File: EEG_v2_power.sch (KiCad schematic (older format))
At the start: 13 parts, among them U2 TLV70033, U3 LM2664, U4 TLV70025, U5 TPS72325

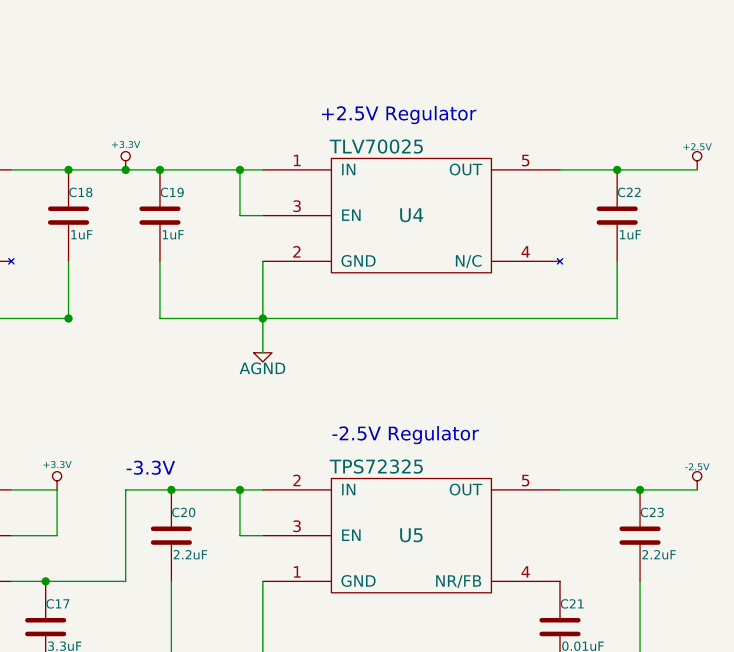
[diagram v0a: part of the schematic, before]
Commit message: Add symbol and footprints for SMD test points.
Add test points to power supplies.
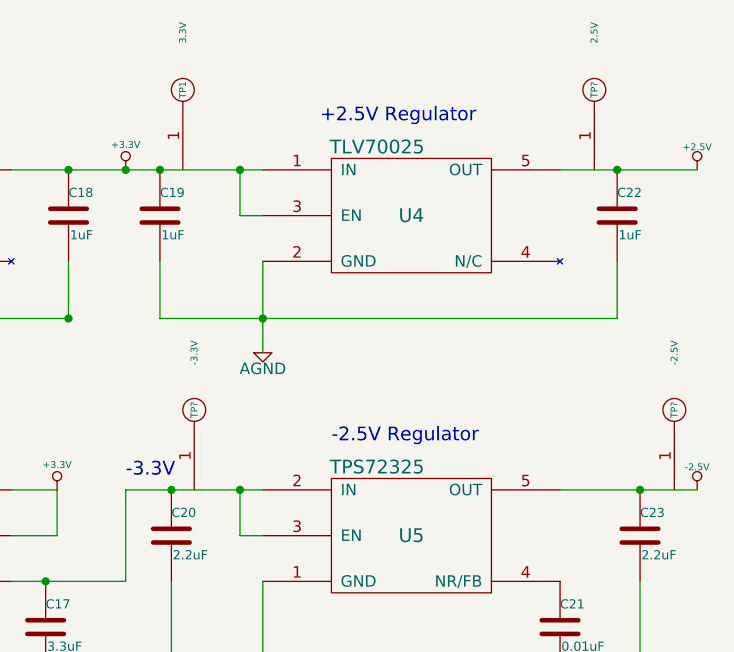
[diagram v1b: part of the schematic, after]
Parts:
- added TP1: 3.3V, ~, symbol SMD_1PIN_PAD
- added TP?: 2.5V, ~, symbol SMD_1PIN_PAD
- added TP?: -3.3V, ~, symbol SMD_1PIN_PAD
- added TP?: -2.5V, ~, symbol SMD_1PIN_PAD
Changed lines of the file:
@@
 +3.3V Regulator
 $Comp
-L +3.3V #PWR19
+L +3.3V #PWR22
 U 1 1 54B47F4F
 P 6450 3050
-F 0 "#PWR19" H 6450 3010 30  0001 C CNN
+F 0 "#PWR22" H 6450 3010 30  0001 C CNN
 F 1 "+3.3V" H 6450 3160 30  0000 C CNN
 F 2 "~" H 6450 3050 60  0000 C CNN
@@
 $EndComp
 $Comp
-L AGND #PWR15
+L AGND #PWR18
 U 1 1 54B47F55
 P 4650 3850
-F 0 "#PWR15" H 4650 3850 40  0001 C CNN
+F 0 "#PWR18" H 4650 3850 40  0001 C CNN
 F 1 "AGND" H 4650 3780 50  0000 C CNN
 F 2 "~" H 4650 3850 60  0000 C CNN
@@
 $EndComp
 $Comp
-L AGND #PWR20
+L AGND #PWR23
 U 1 1 54B47F6D
 P 7050 3850
-F 0 "#PWR20" H 7050 3850 40  0001 C CNN
+F 0 "#PWR23" H 7050 3850 40  0001 C CNN
 F 1 "AGND" H 7050 3780 50  0000 C CNN
 F 2 "~" H 7050 3850 60  0000 C CNN
@@
 $EndComp
 $Comp
-L +2.5V #PWR22
+L +2.5V #PWR25
 U 1 1 54B47F79
 P 8950 3050
-F 0 "#PWR22" H 8950 3000 20  0001 C CNN
+F 0 "#PWR25" H 8950 3000 20  0001 C CNN
 F 1 "+2.5V" H 8950 3150 30  0000 C CNN
 F 2 "" H 8950 3050 60  0000 C CNN
@@
 $EndComp
 $Comp
-L AGND #PWR16
+L AGND #PWR19
 U 1 1 54B47F86
 P 4650 5050
-F 0 "#PWR16" H 4650 5050 40  0001 C CNN
+F 0 "#PWR19" H 4650 5050 40  0001 C CNN
 F 1 "AGND" H 4650 4980 50  0000 C CNN
 F 2 "~" H 4650 5050 60  0000 C CNN
@@
 $EndComp
 $Comp
-L AGND #PWR17
+L AGND #PWR20
 U 1 1 54B47F92
 P 6100 5250
-F 0 "#PWR17" H 6100 5250 40  0001 C CNN
+F 0 "#PWR20" H 6100 5250 40  0001 C CNN
 F 1 "AGND" H 6100 5180 50  0000 C CNN
 F 2 "~" H 6100 5250 60  0000 C CNN
@@
 $EndComp
 $Comp
-L +3.3V #PWR18
+L +3.3V #PWR21
 U 1 1 54B47F98
 P 6150 4450
-F 0 "#PWR18" H 6150 4410 30  0001 C CNN
+F 0 "#PWR21" H 6150 4410 30  0001 C CNN
 F 1 "+3.3V" H 6150 4560 30  0000 C CNN
 F 2 "~" H 6150 4450 60  0000 C CNN
@@
 $EndComp
 $Comp
-L AGND #PWR21
+L AGND #PWR24
 U 1 1 54B47FB2
 P 7650 5350
-F 0 "#PWR21" H 7650 5350 40  0001 C CNN
+F 0 "#PWR24" H 7650 5350 40  0001 C CNN
 F 1 "AGND" H 7650 5280 50  0000 C CNN
 F 2 "~" H 7650 5350 60  0000 C CNN
@@
 $EndComp
 $Comp
-L -2.5V #PWR23
+L -2.5V #PWR26
 U 1 1 54B47FB8
 P 8950 4450
-F 0 "#PWR23" H 8950 4400 20  0001 C CNN
+F 0 "#PWR26" H 8950 4400 20  0001 C CNN
 F 1 "-2.5V" H 8950 4550 30  0000 C CNN
 F 2 "" H 8950 4450 60  0000 C CNN
@@
 Text HLabel 2950 3050 0    60   UnSpc ~ 0
 VIN_RAW
+$Comp
+L SMD_1PIN_PAD TP1
+U 1 1 54C4B7B8
+P 6700 2700
+F 0 "TP1" H 6700 2700 30  0000 C CNN
+F 1 "3.3V" H 6950 2700 30  0000 C CNN
+F 2 "~" H 6700 2700 60  0000 C CNN
+F 3 "~" H 6700 2700 60  0000 C CNN
+	1    6700 2700
+	0    -1   -1   0
+$EndComp
+$Comp
+L SMD_1PIN_PAD TP?
+U 1 1 54C4B7DE
+P 8500 2700
+F 0 "TP?" H 8500 2700 30  0000 C CNN
+F 1 "2.5V" H 8750 2700 30  0000 C CNN
+F 2 "~" H 8500 2700 60  0000 C CNN
+F 3 "~" H 8500 2700 60  0000 C CNN
+	1    8500 2700
+	0    -1   -1   0
+$EndComp
+$Comp
+L SMD_1PIN_PAD TP?
+U 1 1 54C4B7E9
+P 6750 4100
+F 0 "TP?" H 6750 4100 30  0000 C CNN
+F 1 "-3.3V" H 7000 4100 30  0000 C CNN
+F 2 "~" H 6750 4100 60  0000 C CNN
+F 3 "~" H 6750 4100 60  0000 C CNN
+	1    6750 4100
+	0    -1   -1   0
+$EndComp
+$Comp
+L SMD_1PIN_PAD TP?
+U 1 1 54C4B7F4
+P 8850 4100
+F 0 "TP?" H 8850 4100 30  0000 C CNN
+F 1 "-2.5V" H 9100 4100 30  0000 C CNN
+F 2 "~" H 8850 4100 60  0000 C CNN
+F 3 "~" H 8850 4100 60  0000 C CNN
+	1    8850 4100
+	0    -1   -1   0
+$EndComp
 $EndSCHEMATC

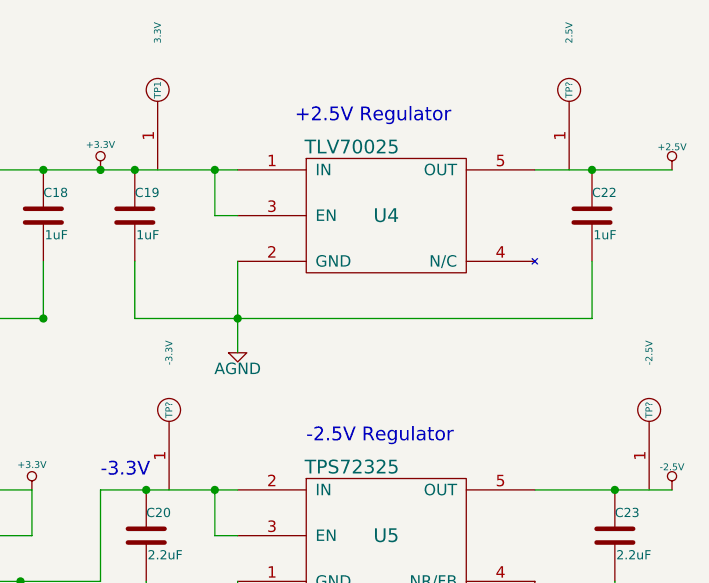
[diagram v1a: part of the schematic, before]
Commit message: Added footprints to ADS caps, shorted unused GPIO to gnd
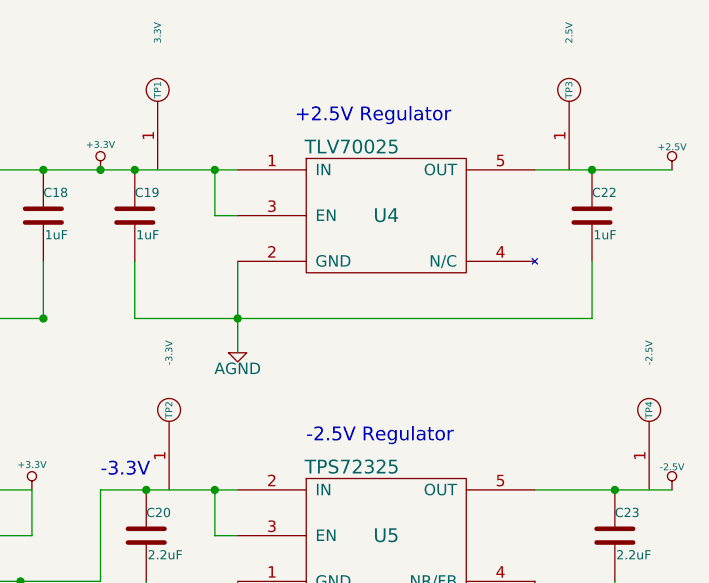
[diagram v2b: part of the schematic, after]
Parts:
- gave numbers to parts that had none: 3
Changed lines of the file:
@@
 +3.3V Regulator
 $Comp
-L +3.3V #PWR22
+L +3.3V #PWR017
 U 1 1 54B47F4F
 P 6450 3050
-F 0 "#PWR22" H 6450 3010 30  0001 C CNN
+F 0 "#PWR017" H 6450 3010 30  0001 C CNN
 F 1 "+3.3V" H 6450 3160 30  0000 C CNN
 F 2 "~" H 6450 3050 60  0000 C CNN
@@
 $EndComp
 $Comp
-L AGND #PWR18
+L AGND #PWR018
 U 1 1 54B47F55
 P 4650 3850
-F 0 "#PWR18" H 4650 3850 40  0001 C CNN
+F 0 "#PWR018" H 4650 3850 40  0001 C CNN
 F 1 "AGND" H 4650 3780 50  0000 C CNN
 F 2 "~" H 4650 3850 60  0000 C CNN
@@
 $EndComp
 $Comp
-L AGND #PWR23
+L AGND #PWR019
 U 1 1 54B47F6D
 P 7050 3850
-F 0 "#PWR23" H 7050 3850 40  0001 C CNN
+F 0 "#PWR019" H 7050 3850 40  0001 C CNN
 F 1 "AGND" H 7050 3780 50  0000 C CNN
 F 2 "~" H 7050 3850 60  0000 C CNN
@@
 $EndComp
 $Comp
-L +2.5V #PWR25
+L +2.5V #PWR020
 U 1 1 54B47F79
 P 8950 3050
-F 0 "#PWR25" H 8950 3000 20  0001 C CNN
+F 0 "#PWR020" H 8950 3000 20  0001 C CNN
 F 1 "+2.5V" H 8950 3150 30  0000 C CNN
 F 2 "" H 8950 3050 60  0000 C CNN
@@
 $EndComp
 $Comp
-L AGND #PWR19
+L AGND #PWR021
 U 1 1 54B47F86
 P 4650 5050
-F 0 "#PWR19" H 4650 5050 40  0001 C CNN
+F 0 "#PWR021" H 4650 5050 40  0001 C CNN
 F 1 "AGND" H 4650 4980 50  0000 C CNN
 F 2 "~" H 4650 5050 60  0000 C CNN
@@
 $EndComp
 $Comp
-L AGND #PWR20
+L AGND #PWR022
 U 1 1 54B47F92
 P 6100 5250
-F 0 "#PWR20" H 6100 5250 40  0001 C CNN
+F 0 "#PWR022" H 6100 5250 40  0001 C CNN
 F 1 "AGND" H 6100 5180 50  0000 C CNN
 F 2 "~" H 6100 5250 60  0000 C CNN
@@
 $EndComp
 $Comp
-L +3.3V #PWR21
+L +3.3V #PWR023
 U 1 1 54B47F98
 P 6150 4450
-F 0 "#PWR21" H 6150 4410 30  0001 C CNN
+F 0 "#PWR023" H 6150 4410 30  0001 C CNN
 F 1 "+3.3V" H 6150 4560 30  0000 C CNN
 F 2 "~" H 6150 4450 60  0000 C CNN
@@
 $EndComp
 $Comp
-L AGND #PWR24
+L AGND #PWR024
 U 1 1 54B47FB2
 P 7650 5350
-F 0 "#PWR24" H 7650 5350 40  0001 C CNN
+F 0 "#PWR024" H 7650 5350 40  0001 C CNN
 F 1 "AGND" H 7650 5280 50  0000 C CNN
 F 2 "~" H 7650 5350 60  0000 C CNN
@@
 $EndComp
 $Comp
-L -2.5V #PWR26
+L -2.5V #PWR025
 U 1 1 54B47FB8
 P 8950 4450
-F 0 "#PWR26" H 8950 4400 20  0001 C CNN
+F 0 "#PWR025" H 8950 4400 20  0001 C CNN
 F 1 "-2.5V" H 8950 4550 30  0000 C CNN
 F 2 "" H 8950 4450 60  0000 C CNN
@@
 $EndComp
 $Comp
-L SMD_1PIN_PAD TP?
+L SMD_1PIN_PAD TP3
 U 1 1 54C4B7DE
 P 8500 2700
-F 0 "TP?" H 8500 2700 30  0000 C CNN
+F 0 "TP3" H 8500 2700 30  0000 C CNN
 F 1 "2.5V" H 8750 2700 30  0000 C CNN
 F 2 "~" H 8500 2700 60  0000 C CNN
@@
 $EndComp
 $Comp
-L SMD_1PIN_PAD TP?
+L SMD_1PIN_PAD TP2
 U 1 1 54C4B7E9
 P 6750 4100
-F 0 "TP?" H 6750 4100 30  0000 C CNN
+F 0 "TP2" H 6750 4100 30  0000 C CNN
 F 1 "-3.3V" H 7000 4100 30  0000 C CNN
 F 2 "~" H 6750 4100 60  0000 C CNN
@@
 $EndComp
 $Comp
-L SMD_1PIN_PAD TP?
+L SMD_1PIN_PAD TP4
 U 1 1 54C4B7F4
 P 8850 4100
-F 0 "TP?" H 8850 4100 30  0000 C CNN
+F 0 "TP4" H 8850 4100 30  0000 C CNN
 F 1 "-2.5V" H 9100 4100 30  0000 C CNN
 F 2 "~" H 8850 4100 60  0000 C CNN

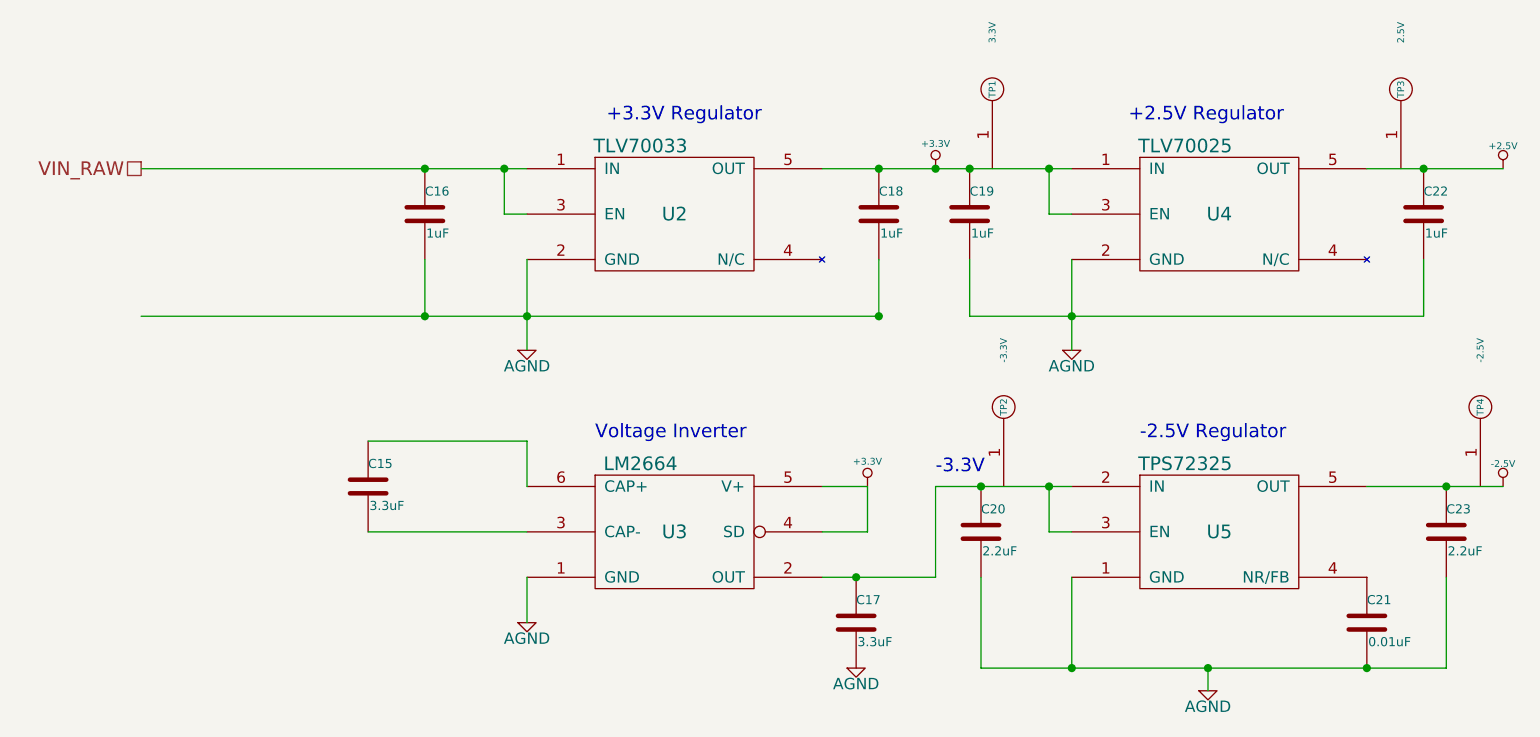
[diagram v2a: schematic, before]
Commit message: Clean ERC errors.
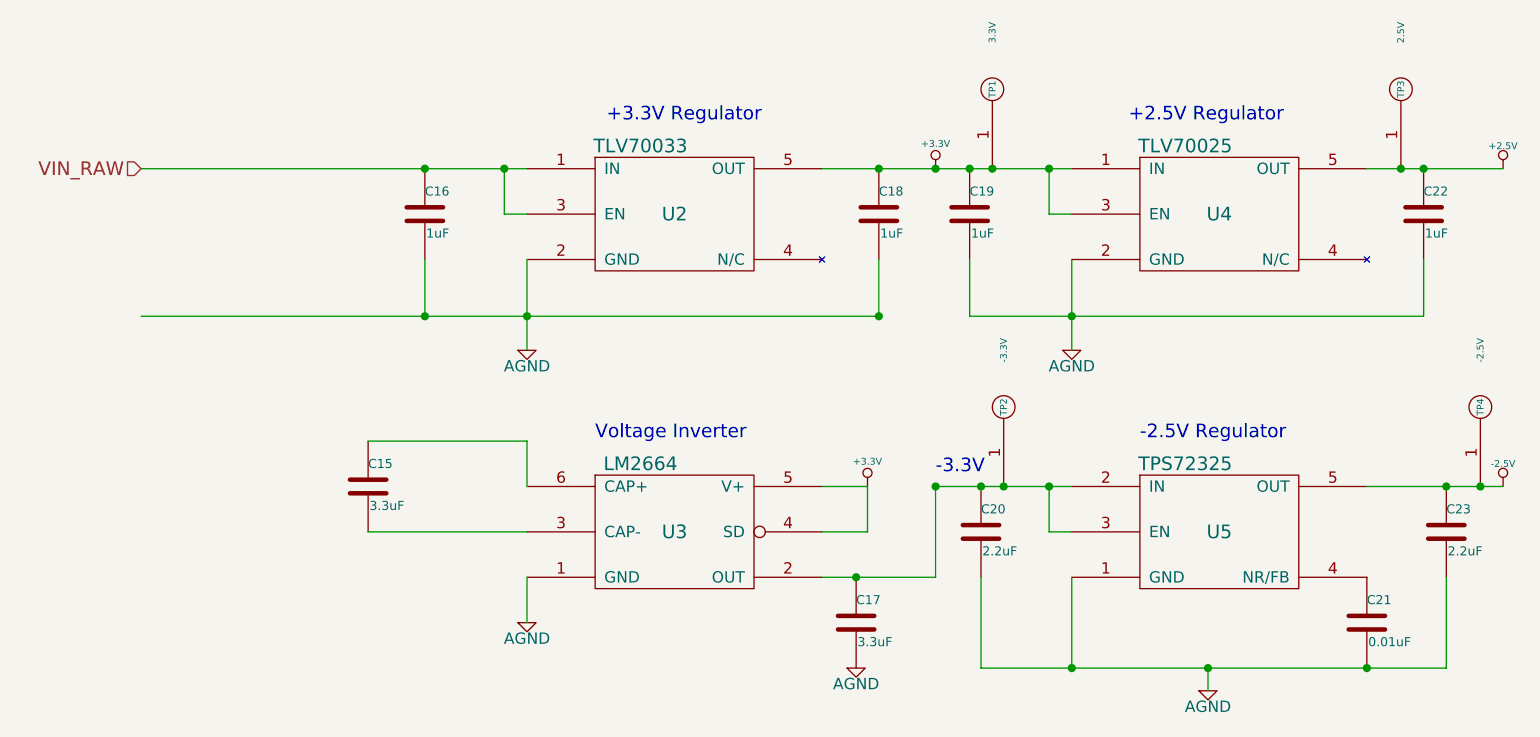
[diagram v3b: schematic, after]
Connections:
- net +2.5V: now also TP3.1
- net +3.3V: now also TP1.1
- net -2.5V: now also TP4.1
- net at C17.1, C20.1, U3.2 (OUT)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: now also TP2.1
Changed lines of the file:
@@
 +3.3V Regulator
 $Comp
-L +3.3V #PWR017
+L +3.3V #PWR020
 U 1 1 54B47F4F
 P 6450 3050
-F 0 "#PWR017" H 6450 3010 30  0001 C CNN
+F 0 "#PWR020" H 6450 3010 30  0001 C CNN
 F 1 "+3.3V" H 6450 3160 30  0000 C CNN
 F 2 "~" H 6450 3050 60  0000 C CNN
@@
 $EndComp
 $Comp
-L AGND #PWR018
+L AGND #PWR021
 U 1 1 54B47F55
 P 4650 3850
-F 0 "#PWR018" H 4650 3850 40  0001 C CNN
+F 0 "#PWR021" H 4650 3850 40  0001 C CNN
 F 1 "AGND" H 4650 3780 50  0000 C CNN
 F 2 "~" H 4650 3850 60  0000 C CNN
@@
 $EndComp
 $Comp
-L AGND #PWR019
+L AGND #PWR022
 U 1 1 54B47F6D
 P 7050 3850
-F 0 "#PWR019" H 7050 3850 40  0001 C CNN
+F 0 "#PWR022" H 7050 3850 40  0001 C CNN
 F 1 "AGND" H 7050 3780 50  0000 C CNN
 F 2 "~" H 7050 3850 60  0000 C CNN
@@
 $EndComp
 $Comp
-L +2.5V #PWR020
+L +2.5V #PWR023
 U 1 1 54B47F79
 P 8950 3050
-F 0 "#PWR020" H 8950 3000 20  0001 C CNN
+F 0 "#PWR023" H 8950 3000 20  0001 C CNN
 F 1 "+2.5V" H 8950 3150 30  0000 C CNN
 F 2 "" H 8950 3050 60  0000 C CNN
@@
 $EndComp
 $Comp
-L AGND #PWR021
+L AGND #PWR024
 U 1 1 54B47F86
 P 4650 5050
-F 0 "#PWR021" H 4650 5050 40  0001 C CNN
+F 0 "#PWR024" H 4650 5050 40  0001 C CNN
 F 1 "AGND" H 4650 4980 50  0000 C CNN
 F 2 "~" H 4650 5050 60  0000 C CNN
@@
 $EndComp
 $Comp
-L AGND #PWR022
+L AGND #PWR025
 U 1 1 54B47F92
 P 6100 5250
-F 0 "#PWR022" H 6100 5250 40  0001 C CNN
+F 0 "#PWR025" H 6100 5250 40  0001 C CNN
 F 1 "AGND" H 6100 5180 50  0000 C CNN
 F 2 "~" H 6100 5250 60  0000 C CNN
@@
 $EndComp
 $Comp
-L +3.3V #PWR023
+L +3.3V #PWR026
 U 1 1 54B47F98
 P 6150 4450
-F 0 "#PWR023" H 6150 4410 30  0001 C CNN
+F 0 "#PWR026" H 6150 4410 30  0001 C CNN
 F 1 "+3.3V" H 6150 4560 30  0000 C CNN
 F 2 "~" H 6150 4450 60  0000 C CNN
@@
 $EndComp
 $Comp
-L AGND #PWR024
+L AGND #PWR027
 U 1 1 54B47FB2
 P 7650 5350
-F 0 "#PWR024" H 7650 5350 40  0001 C CNN
+F 0 "#PWR027" H 7650 5350 40  0001 C CNN
 F 1 "AGND" H 7650 5280 50  0000 C CNN
 F 2 "~" H 7650 5350 60  0000 C CNN
@@
 $EndComp
 $Comp
-L -2.5V #PWR025
+L -2.5V #PWR028
 U 1 1 54B47FB8
 P 8950 4450
-F 0 "#PWR025" H 8950 4400 20  0001 C CNN
+F 0 "#PWR028" H 8950 4400 20  0001 C CNN
 F 1 "-2.5V" H 8950 4550 30  0000 C CNN
 F 2 "" H 8950 4450 60  0000 C CNN
@@
 	4550 3250 4650 3250
 Connection ~ 4550 3050
-Wire Wire Line
-	2950 3050 4650 3050
 Connection ~ 4200 3050
 Wire Wire Line
@@
 	6950 3250 7050 3250
 Connection ~ 6950 3050
-Wire Wire Line
-	8350 3050 8950 3050
 Connection ~ 8600 3050
 Wire Wire Line
@@
 	8700 5250 8700 4850
 Connection ~ 8350 5250
-Wire Wire Line
-	8350 4450 8950 4450
 Connection ~ 8700 4450
 Wire Wire Line
@@
 Connection ~ 7050 5250
 Connection ~ 4200 3700
-Wire Wire Line
-	6450 4450 7050 4450
 Connection ~ 6650 4450
-Wire Wire Line
-	5950 3050 7050 3050
 Connection ~ 6600 3050
 Wire Wire Line
@@
 Wire Wire Line
 	6150 4450 6150 4650
-Text HLabel 2950 3050 0    60   UnSpc ~ 0
+Text HLabel 2950 3050 0    60   Input ~ 0
 VIN_RAW
 $Comp
@@
 	0    -1   -1   0
 $EndComp
+Wire Wire Line
+	5950 3050 7050 3050
+Connection ~ 6700 3050
+Wire Wire Line
+	8350 3050 8950 3050
+Connection ~ 8500 3050
+Wire Wire Line
+	8350 4450 8950 4450
+Connection ~ 8850 4450
+Connection ~ 6450 4450
+Connection ~ 6750 4450
+Wire Wire Line
+	6450 4450 7050 4450
+Wire Wire Line
+	2950 3050 4650 3050
 $EndSCHEMATC

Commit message: Modify libraries to be correct. Add pushbuttons and LEDs. Change switch to toggle.
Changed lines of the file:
@@
 Sheet 3 4
 Title "Project Synapse Prototype Board"
-Date "27 jan 2015"
+Date "28 jan 2015"
 Rev "A.b"
 Comp "Senior Design 14-15"
@@
 +3.3V Regulator
 $Comp
-L +3.3V #PWR021
+L +3.3V #PWR029
 U 1 1 54B47F4F
 P 6450 3050
-F 0 "#PWR021" H 6450 3010 30  0001 C CNN
+F 0 "#PWR029" H 6450 3010 30  0001 C CNN
 F 1 "+3.3V" H 6450 3160 30  0000 C CNN
 F 2 "~" H 6450 3050 60  0000 C CNN
@@
 $EndComp
 $Comp
-L AGND #PWR022
+L AGND #PWR030
 U 1 1 54B47F55
 P 4650 3850
-F 0 "#PWR022" H 4650 3850 40  0001 C CNN
+F 0 "#PWR030" H 4650 3850 40  0001 C CNN
 F 1 "AGND" H 4650 3780 50  0000 C CNN
 F 2 "~" H 4650 3850 60  0000 C CNN
@@
 $EndComp
 $Comp
-L AGND #PWR023
+L AGND #PWR031
 U 1 1 54B47F6D
 P 7050 3850
-F 0 "#PWR023" H 7050 3850 40  0001 C CNN
+F 0 "#PWR031" H 7050 3850 40  0001 C CNN
 F 1 "AGND" H 7050 3780 50  0000 C CNN
 F 2 "~" H 7050 3850 60  0000 C CNN
@@
 $EndComp
 $Comp
-L +2.5V #PWR024
+L +2.5V #PWR032
 U 1 1 54B47F79
 P 8950 3050
-F 0 "#PWR024" H 8950 3000 20  0001 C CNN
+F 0 "#PWR032" H 8950 3000 20  0001 C CNN
 F 1 "+2.5V" H 8950 3150 30  0000 C CNN
 F 2 "" H 8950 3050 60  0000 C CNN
@@
 $EndComp
 $Comp
-L AGND #PWR025
+L AGND #PWR033
 U 1 1 54B47F86
 P 4650 5050
-F 0 "#PWR025" H 4650 5050 40  0001 C CNN
+F 0 "#PWR033" H 4650 5050 40  0001 C CNN
 F 1 "AGND" H 4650 4980 50  0000 C CNN
 F 2 "~" H 4650 5050 60  0000 C CNN
@@
 $EndComp
 $Comp
-L AGND #PWR026
+L AGND #PWR034
 U 1 1 54B47F92
 P 6100 5250
-F 0 "#PWR026" H 6100 5250 40  0001 C CNN
+F 0 "#PWR034" H 6100 5250 40  0001 C CNN
 F 1 "AGND" H 6100 5180 50  0000 C CNN
 F 2 "~" H 6100 5250 60  0000 C CNN
@@
 $EndComp
 $Comp
-L +3.3V #PWR027
+L +3.3V #PWR035
 U 1 1 54B47F98
 P 6150 4450
-F 0 "#PWR027" H 6150 4410 30  0001 C CNN
+F 0 "#PWR035" H 6150 4410 30  0001 C CNN
 F 1 "+3.3V" H 6150 4560 30  0000 C CNN
 F 2 "~" H 6150 4450 60  0000 C CNN
@@
 $EndComp
 $Comp
-L AGND #PWR028
+L AGND #PWR036
 U 1 1 54B47FB2
 P 7650 5350
-F 0 "#PWR028" H 7650 5350 40  0001 C CNN
+F 0 "#PWR036" H 7650 5350 40  0001 C CNN
 F 1 "AGND" H 7650 5280 50  0000 C CNN
 F 2 "~" H 7650 5350 60  0000 C CNN
@@
 $EndComp
 $Comp
-L -2.5V #PWR029
+L -2.5V #PWR037
 U 1 1 54B47FB8
 P 8950 4450
-F 0 "#PWR029" H 8950 4400 20  0001 C CNN
+F 0 "#PWR037" H 8950 4400 20  0001 C CNN
 F 1 "-2.5V" H 8950 4550 30  0000 C CNN
 F 2 "" H 8950 4450 60  0000 C CNN
@@
 -2.5V Regulator
 Wire Wire Line
-	4550 3050 4550 3250
-Wire Wire Line
 	4550 3250 4650 3250
-Connection ~ 4550 3050
 Connection ~ 4200 3050
 Wire Wire Line
@@
 Wire Wire Line
 	2950 3050 4650 3050
+Wire Wire Line
+	4550 3250 4550 3050
+Connection ~ 4550 3050
 $EndSCHEMATC
